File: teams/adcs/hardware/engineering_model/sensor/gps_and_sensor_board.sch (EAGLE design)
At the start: 35 parts, among them U1 LINEAR_LDO_LT1761-X, U2 LINEAR_LDO_LT1761-X, U3 OEM719, U4 LTC3624

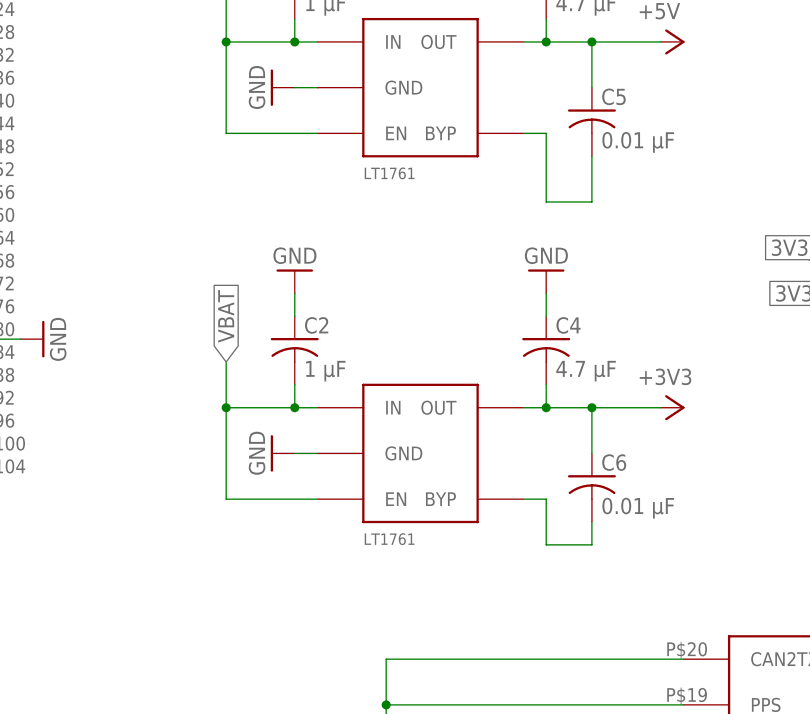
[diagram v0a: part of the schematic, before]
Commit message: ADCS/GPS: Updated outdated library components
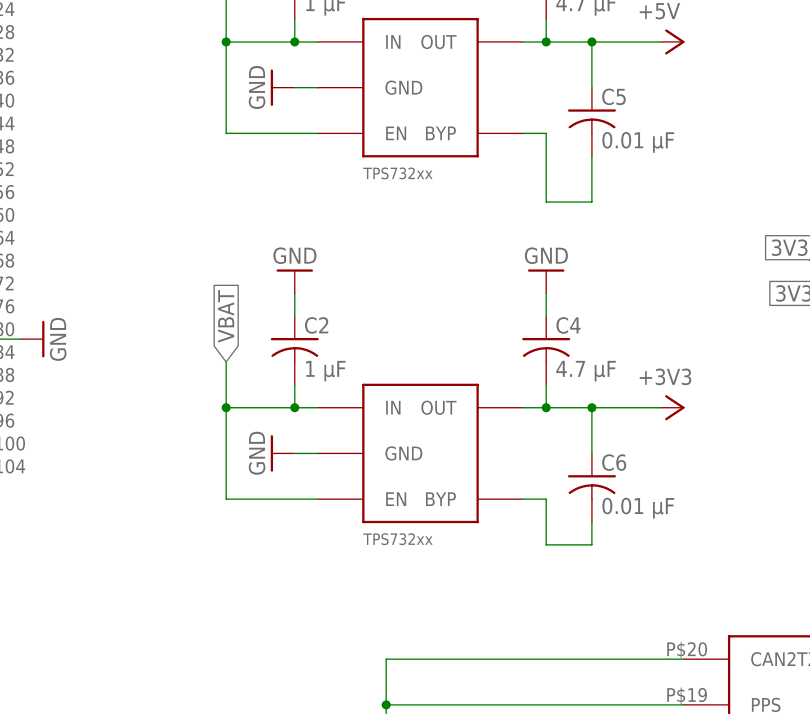
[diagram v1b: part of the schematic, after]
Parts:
- U1, U2: value LINEAR_LDO_LT1761-X -> TPS732XX; device DubSat1 Components:LINEAR_LDO_LT1761-X -> DubSat1 Components:TPS732XX
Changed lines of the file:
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@@
 <part name="GND2" library="supply1" library_urn="urn:adsk.eagle:library:371" deviceset="GND" device=""/>
 <part name="GND3" library="supply1" library_urn="urn:adsk.eagle:library:371" deviceset="GND" device=""/>
-<part name="U1" library="DubSat1 Components" deviceset="LINEAR_LDO_LT1761-X" device=""/>
+<part name="U1" library="DubSat1 Components" deviceset="TPS732XX" device=""/>
 <part name="GND7" library="supply1" library_urn="urn:adsk.eagle:library:371" deviceset="GND" device=""/>
 <part name="P+2" library="supply1" library_urn="urn:adsk.eagle:library:371" deviceset="+5V" device=""/>
@@
 <part name="C3" library="rcl" library_urn="urn:adsk.eagle:library:334" deviceset="C-US" device="C0805" package3d_urn="urn:adsk.eagle:package:23617/2" value="4.7 μF"/>
 <part name="GND11" library="supply1" library_urn="urn:adsk.eagle:library:371" deviceset="GND" device=""/>
-<part name="U2" library="DubSat1 Components" deviceset="LINEAR_LDO_LT1761-X" device=""/>
+<part name="U2" library="DubSat1 Components" deviceset="TPS732XX" device=""/>
 <part name="GND8" library="supply1" library_urn="urn:adsk.eagle:library:371" deviceset="GND" device=""/>
 <part name="+3V36" library="supply1" library_urn="urn:adsk.eagle:library:371" deviceset="+3V3" device=""/>

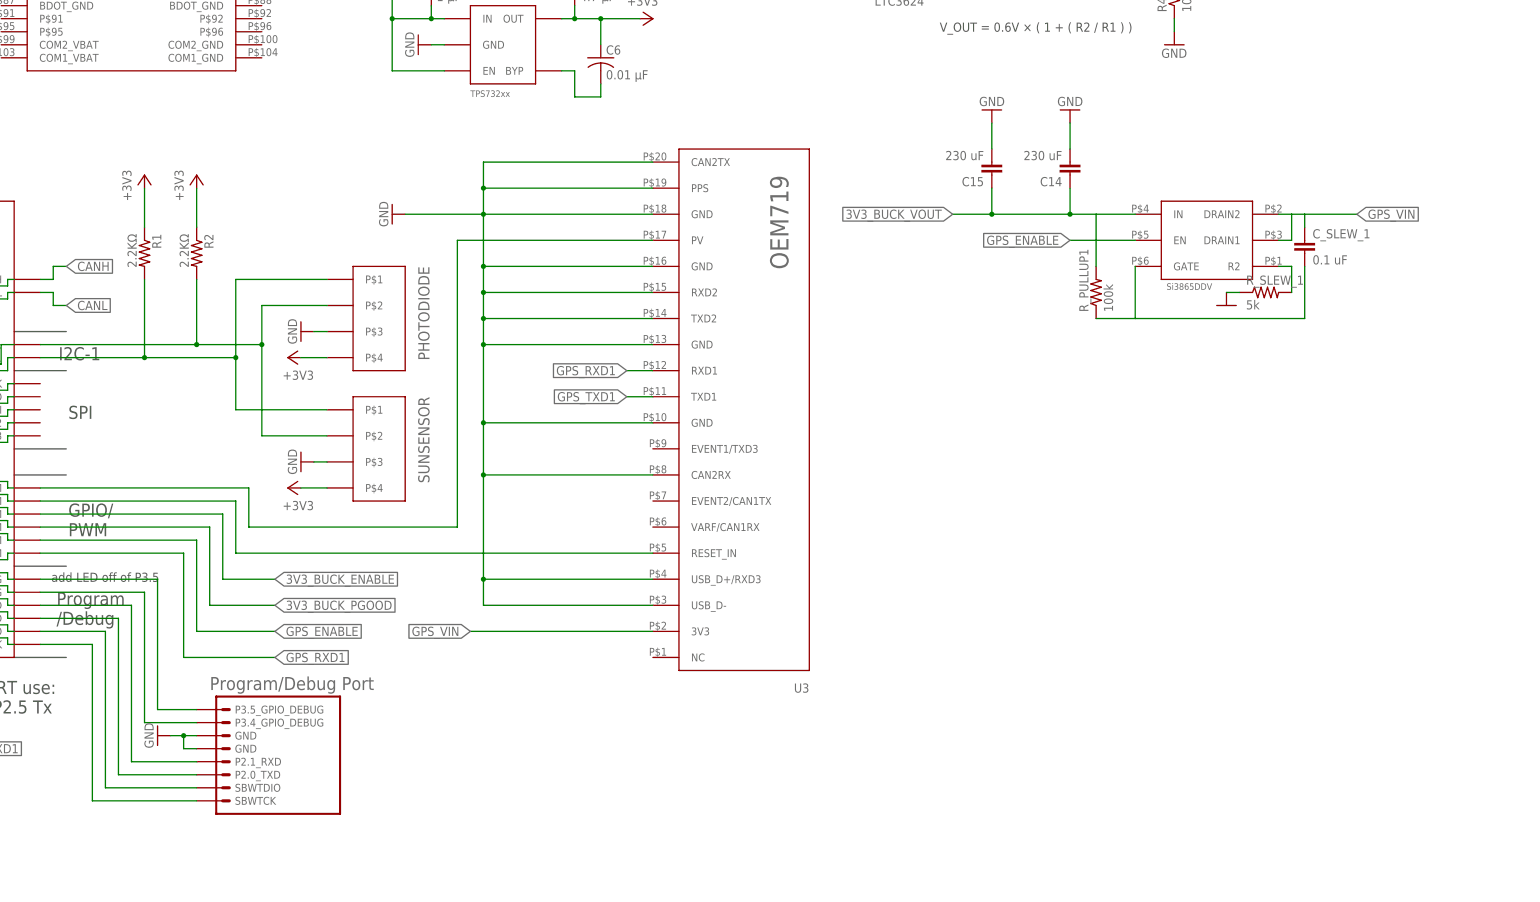
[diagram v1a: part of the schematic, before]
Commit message: ADCS/GPS: Add LED to GPIO 3.5
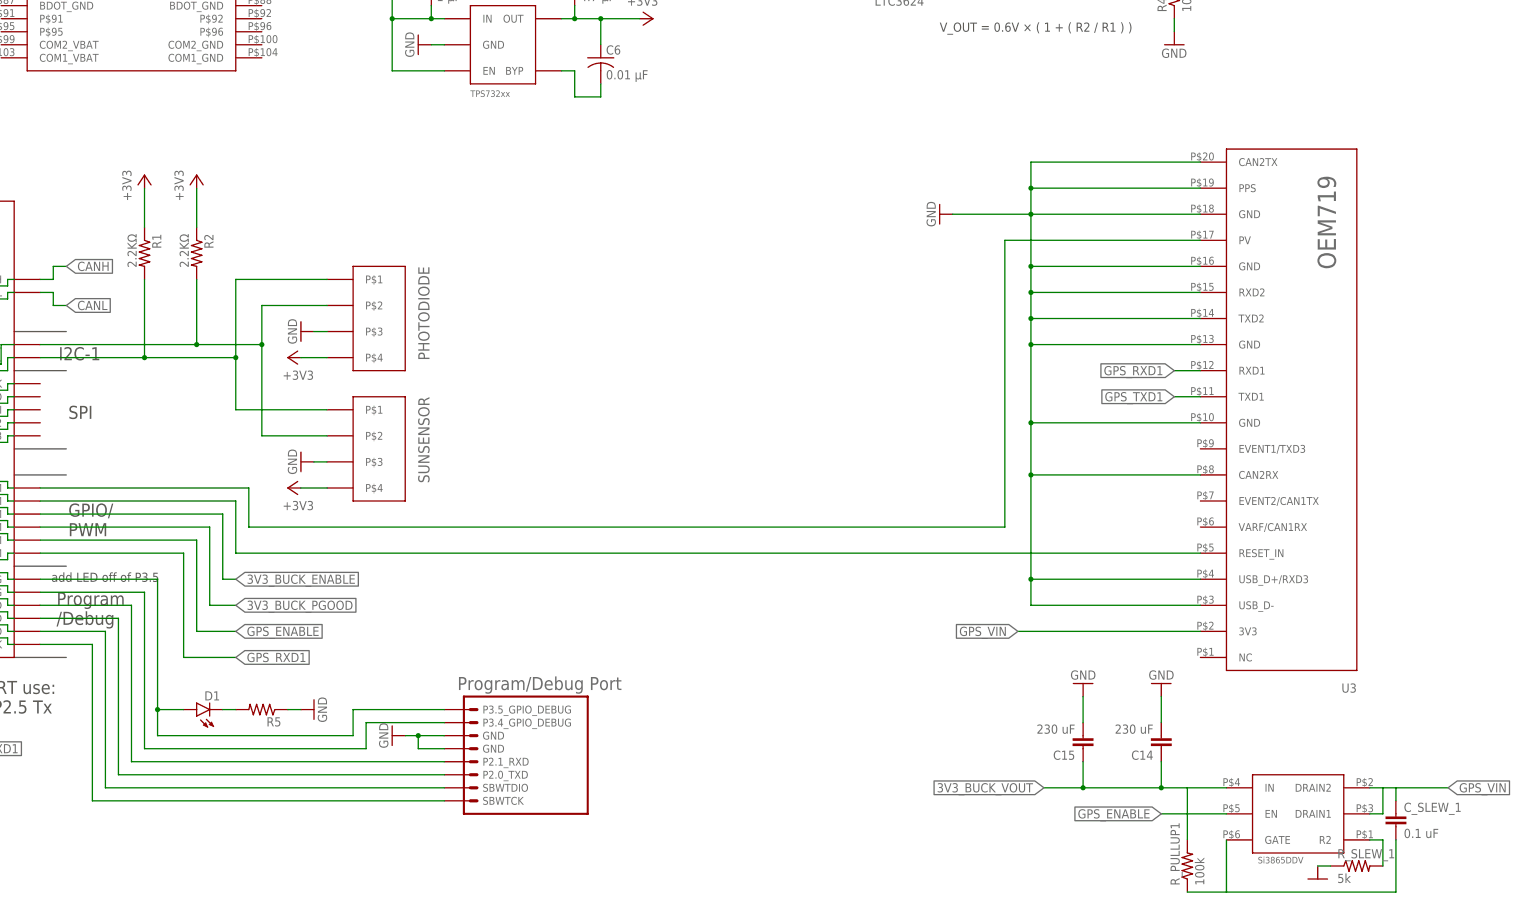
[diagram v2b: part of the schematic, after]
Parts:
- added D1: (no value), DubSat1 Components:LED
- added R5: (no value), DubSat1 Components:RESISTOR0805
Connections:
- new net N$9: D1.C, R5.2
- net GND: now also R5.1
- net N$1: now also D1.A
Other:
- moved on the sheet: C14, C15, C_SLEW_1, R_PULLUP1, R_SLEW_1, U3

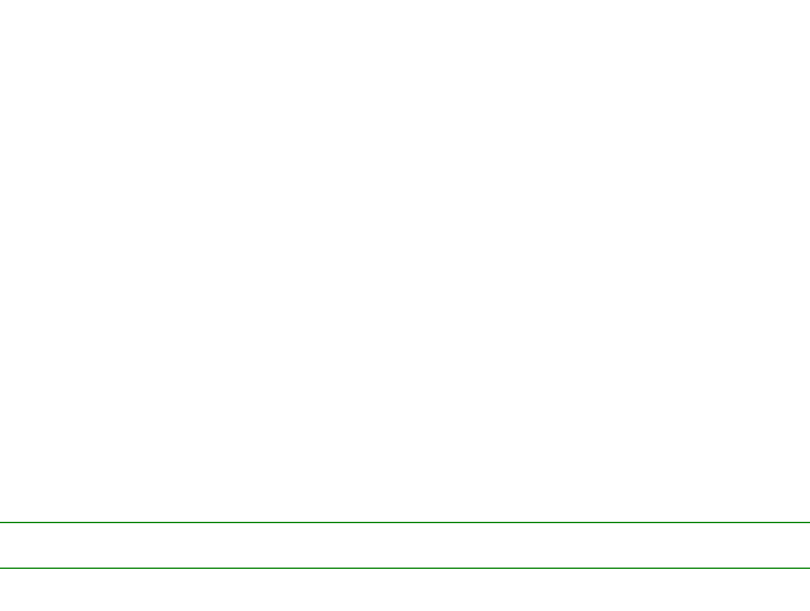
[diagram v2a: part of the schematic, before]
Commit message: ADCS/GPS: Add debug header for GPS UART, PV, and RESET pins
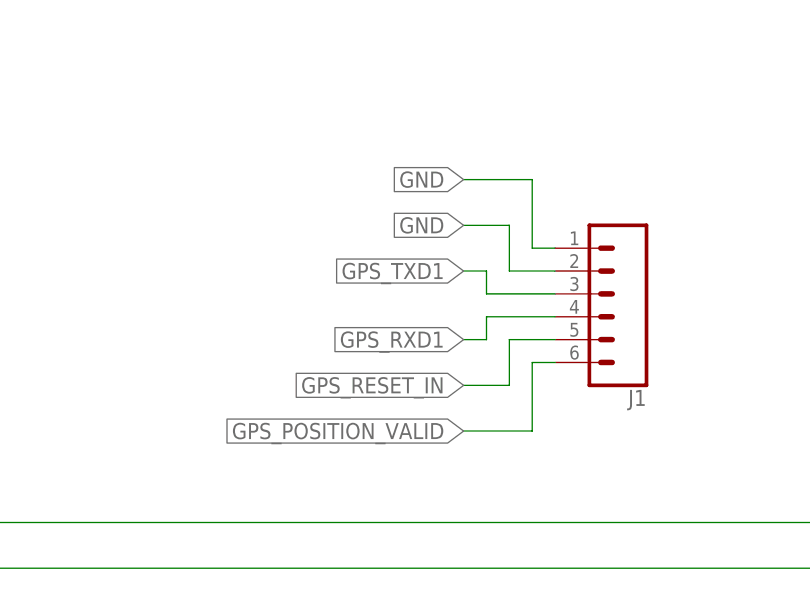
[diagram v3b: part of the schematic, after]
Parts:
- added J1: (no value), SparkFun-Connectors:CONN_06LOCK
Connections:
- net GND: now also J1.1, J1.2
- net GPS_POSITION_VALID: now also J1.6
- net GPS_RESET_IN: now also J1.5
- net GPS_RXD1: now also J1.4
- net GPS_TXD1: now also J1.3
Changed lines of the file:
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@@
 <part name="R5" library="DubSat1 Components" deviceset="RESISTOR" device="0805"/>
 <part name="GND20" library="supply1" library_urn="urn:adsk.eagle:library:371" deviceset="GND" device=""/>
+<part name="J1" library="SparkFun-Connectors" deviceset="CONN_06" device="LOCK"/>
 </parts>
 <sheets>
@@
 <instance part="R5" gate="G$1" x="119.38" y="-127" rot="R180"/>
 <instance part="GND20" gate="1" x="129.54" y="-127" rot="R90"/>
+<instance part="J1" gate="G$1" x="236.22" y="-66.04" rot="R180"/>
 </instances>
 <busses>
@@
 <wire x1="124.46" y1="-127" x2="127" y2="-127" width="0.1524" layer="91"/>
 </segment>
+<segment>
+<pinref part="J1" gate="G$1" pin="1"/>
+<wire x1="231.14" y1="-60.96" x2="228.6" y2="-60.96" width="0.1524" layer="91"/>
+<wire x1="228.6" y1="-60.96" x2="228.6" y2="-53.34" width="0.1524" layer="91"/>
+<wire x1="228.6" y1="-53.34" x2="220.98" y2="-53.34" width="0.1524" layer="91"/>
+<label x="220.98" y="-53.34" size="1.778" layer="95" rot="R180" xref="yes"/>
+</segment>
+<segment>
+<pinref part="J1" gate="G$1" pin="2"/>
+<wire x1="231.14" y1="-63.5" x2="226.06" y2="-63.5" width="0.1524" layer="91"/>
+<wire x1="226.06" y1="-63.5" x2="226.06" y2="-58.42" width="0.1524" layer="91"/>
+<wire x1="226.06" y1="-58.42" x2="220.98" y2="-58.42" width="0.1524" layer="91"/>
+<label x="220.98" y="-58.42" size="1.778" layer="95" rot="R180" xref="yes"/>
+</segment>
 </net>
 <net name="VBAT" class="0">
@@
 <pinref part="BLK1" gate="G$1" pin="P1.7_GPIO/PWM"/>
 <wire x1="116.84" y1="-83.82" x2="76.2" y2="-83.82" width="0.1524" layer="91"/>
+</segment>
+<segment>
+<pinref part="J1" gate="G$1" pin="6"/>
+<wire x1="231.14" y1="-73.66" x2="228.6" y2="-73.66" width="0.1524" layer="91"/>
+<wire x1="228.6" y1="-73.66" x2="228.6" y2="-81.28" width="0.1524" layer="91"/>
+<wire x1="228.6" y1="-81.28" x2="220.98" y2="-81.28" width="0.1524" layer="91"/>
+<label x="220.98" y="-81.28" size="1.778" layer="95" rot="R180" xref="yes"/>
 </segment>
 </net>
@@
 <wire x1="114.3" y1="-86.36" x2="76.2" y2="-86.36" width="0.1524" layer="91"/>
 </segment>
+<segment>
+<pinref part="J1" gate="G$1" pin="5"/>
+<wire x1="231.14" y1="-71.12" x2="226.06" y2="-71.12" width="0.1524" layer="91"/>
+<wire x1="226.06" y1="-71.12" x2="226.06" y2="-76.2" width="0.1524" layer="91"/>
+<wire x1="226.06" y1="-76.2" x2="220.98" y2="-76.2" width="0.1524" layer="91"/>
+<label x="220.98" y="-76.2" size="1.778" layer="95" rot="R180" xref="yes"/>
+</segment>
 </net>
 <net name="GPS_VIN" class="0">
@@
 <wire x1="104.14" y1="-116.84" x2="114.3" y2="-116.84" width="0.1524" layer="91"/>
 </segment>
+<segment>
+<pinref part="J1" gate="G$1" pin="4"/>
+<wire x1="231.14" y1="-68.58" x2="223.52" y2="-68.58" width="0.1524" layer="91"/>
+<wire x1="223.52" y1="-68.58" x2="223.52" y2="-71.12" width="0.1524" layer="91"/>
+<wire x1="223.52" y1="-71.12" x2="220.98" y2="-71.12" width="0.1524" layer="91"/>
+<label x="220.98" y="-71.12" size="1.778" layer="95" rot="R180" xref="yes"/>
+</segment>
 </net>
 <net name="GPS_TXD1" class="0">
@@
 <label x="58.42" y="-134.62" size="1.778" layer="95" xref="yes"/>
 </segment>
-</net>
+<segment>
+<pinref part="J1" gate="G$1" pin="3"/>
+<wire x1="231.14" y1="-66.04" x2="223.52" y2="-66.04" width="0.1524" layer="91"/>
+<wire x1="223.52" y1="-66.04" x2="223.52" y2="-63.5" width="0.1524" layer="91"/>
+<wire x1="223.52" y1="-63.5" x2="220.98" y2="-63.5" width="0.1524" layer="91"/>
+<label x="220.98" y="-63.5" size="1.778" layer="95" rot="R180" xref="yes"/>
+</segment>
+</net>

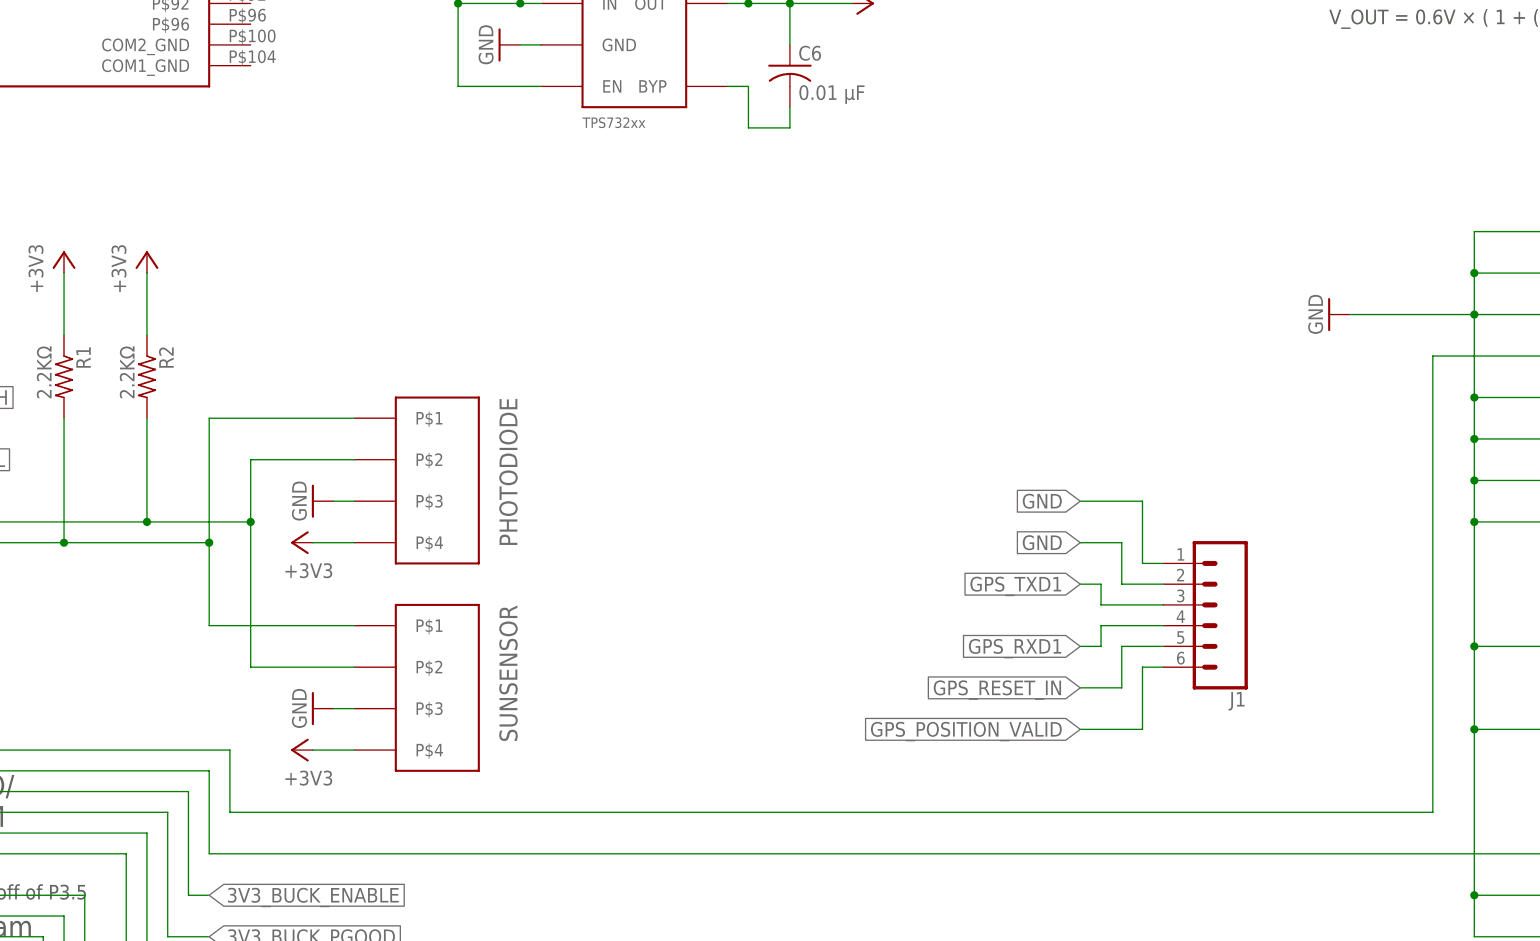
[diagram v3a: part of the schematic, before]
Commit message: ADCS/GPS: Add debug jumpers for all I2C devices
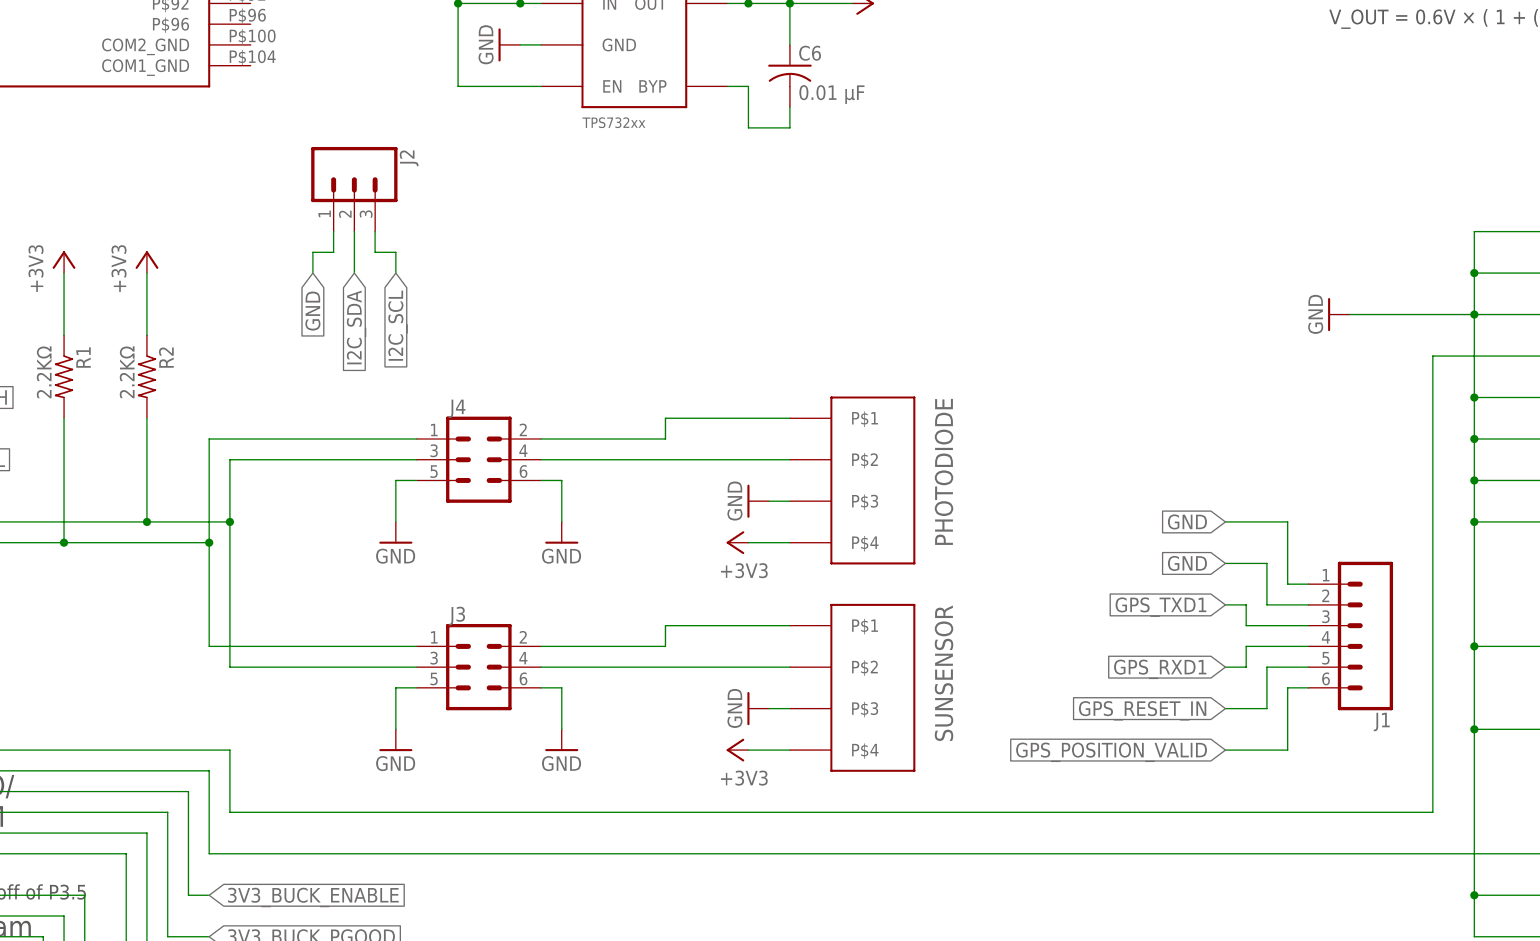
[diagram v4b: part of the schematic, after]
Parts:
- added J2: (no value), SparkFun-Connectors:CONN_03LOCK
- added J3, J4: (no value), SparkFun-Connectors:CONN_03X22X3_SILK_MALE_PTH
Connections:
- new net PHOTODIODE_SCL: J4.4, PHOTODIODE.P$2
- new net PHOTODIODE_SDA: J4.2, PHOTODIODE.P$1
- new net SUNSENSOR_SCL: J3.4, SUNSENSOR.P$2
- new net SUNSENSOR_SDA: J3.2, SUNSENSOR.P$1
- net GND: now also J2.1, J3.5, J3.6, J4.5, J4.6
- net I2C_SCL: now also J2.3, J3.3, J4.3; no longer PHOTODIODE.P$2, SUNSENSOR.P$2
- net I2C_SDA: now also J2.2, J3.1, J4.1; no longer PHOTODIODE.P$1, SUNSENSOR.P$1
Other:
- moved on the sheet: J1, PHOTODIODE, SUNSENSOR
